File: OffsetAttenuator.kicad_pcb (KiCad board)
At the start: 2 copper layers, 17 parts, among them J1 Conn_Coaxial, J2 Conn_Coaxial, SW1 POWER, SW2 BYPASS, U1 L7805, X1 4MHz

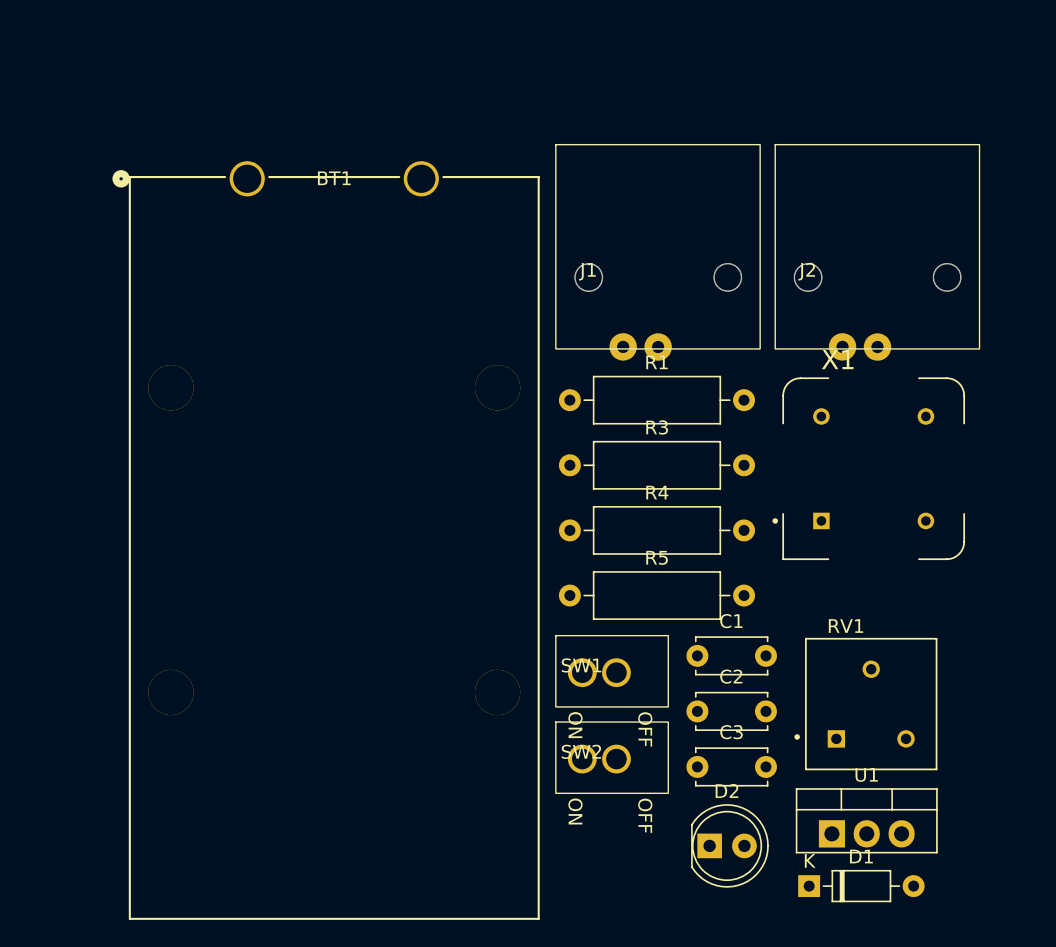
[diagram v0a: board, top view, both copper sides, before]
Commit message: adding osc schematic and footprint
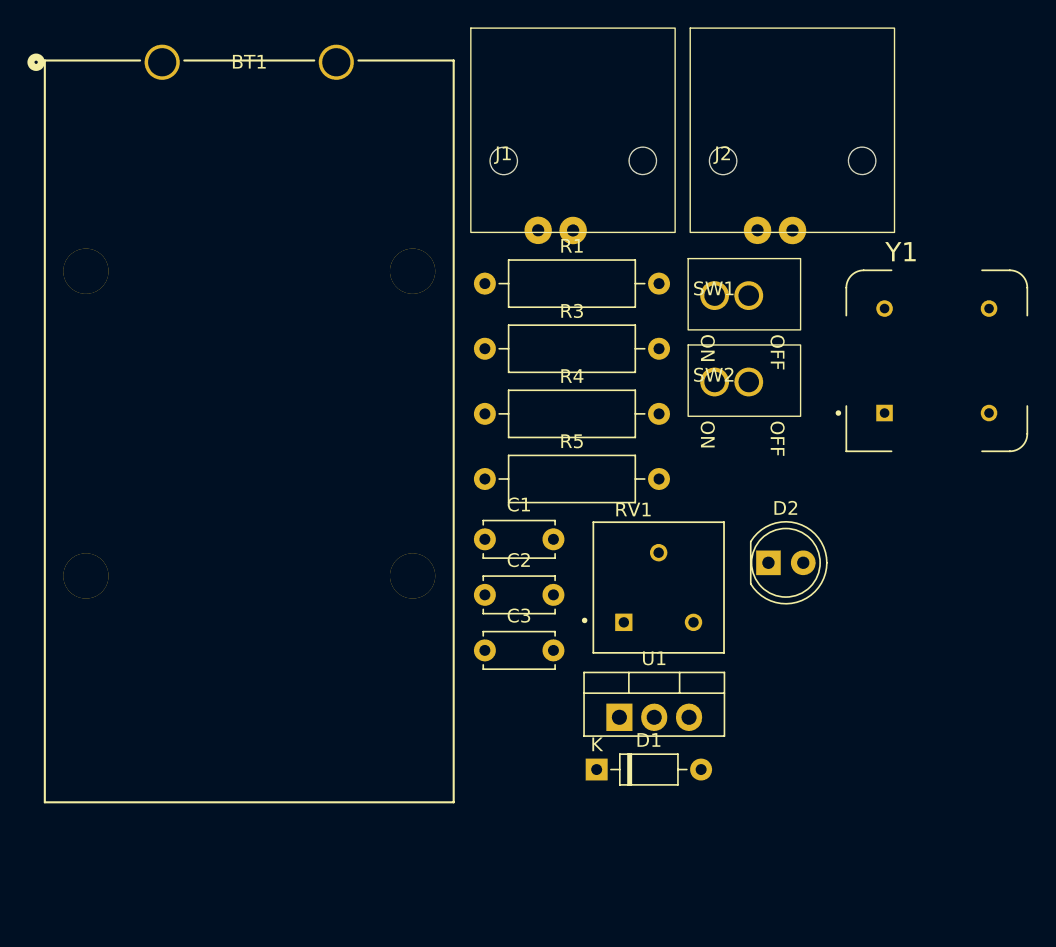
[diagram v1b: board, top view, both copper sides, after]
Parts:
- removed X1: 4MHz, Library:OSC_ECS-2100AX-040
- added Y1: ECS-2100AX-040, Library:OSC_ECS-2100AX-040, F.Cu at (163.2, 83.2)
- moved SW1 29.1 mm to (146.9, 78.4)
- moved SW2 29.1 mm to (146.9, 84.7)
- moved D2 21.1 mm to (150.9, 97.9)
- moved C1 17.7 mm to (130.2, 96.2)
- moved C2 17.7 mm to (130.2, 100.3)
- moved C3 17.7 mm to (130.2, 104.3)
- moved D1 17.7 mm to (138.4, 113.0)
- moved RV1 17.7 mm to (142.9, 99.7)
- moved U1 17.7 mm to (140.0, 109.2)
- moved J1 10.5 mm to (131.6, 68.6)
- moved J2 10.5 mm to (147.6, 68.6)
- moved R1 10.5 mm to (130.2, 77.6)
- moved R3 10.5 mm to (130.2, 82.3)
- moved R4 10.5 mm to (130.2, 87.1)
- moved R5 10.5 mm to (130.2, 91.8)
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
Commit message: begin layout
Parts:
- R4: moved to B.Cu
- moved J1 91.0 mm to (41.8, 54.0), turned to 90 degrees
- moved SW2 86.2 mm to (77.1, 34.2), turned to 90 degrees
- moved C1 80.0 mm to (63.5, 52.0), turned to 90 degrees
- moved SW1 75.8 mm to (78.5, 111.0), turned to 90 degrees
- moved D1 75.7 mm to (100.1, 47.8), turned to 180 degrees
- moved J2 68.7 mm to (211.7, 44.0), turned to -90 degrees
- moved RV1 67.5 mm to (80.5, 74.0)
- moved R1 58.2 mm to (80.5, 47.3), turned to -90 degrees
- moved BT1 57.5 mm to (100.0, 118.5)
- moved R4 53.4 mm to (78.5, 100.2), turned to 90 degrees
- moved C2 52.7 mm to (125.2, 47.8), turned to -90 degrees
- moved R3 40.3 mm to (110.5, 47.1), turned to -90 degrees
- moved D2 37.6 mm to (183.5, 79.0)
- moved R5 37.6 mm to (162.8, 72.9)
- moved Y1 34.5 mm to (133.5, 100.8), turned to 180 degrees
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
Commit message: pcb layout
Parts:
- BT1: moved to B.Cu
- moved J2 93.5 mm to (118.2, 46.2)
- moved D2 92.6 mm to (95.8, 49.2)
- moved BT1 85.4 mm to (50.3, 49.1), turned to -90 degrees
- moved R5 60.2 mm to (104.8, 56.8), turned to -90 degrees
- moved Y1 54.2 mm to (93.8, 63.8)
- moved C3 48.6 mm to (79.8, 73.0)
- moved U1 45.5 mm to (82.8, 66.0), turned to 90 degrees
- moved C2 38.8 mm to (86.8, 52.2), turned to 90 degrees
- moved SW1 36.1 mm to (74.0, 75.2), turned to 180 degrees
- moved R3 31.5 mm to (79.2, 43.5)
- moved R4 31.4 mm to (63.2, 72.7)
- moved D1 28.2 mm to (72.5, 53.6), turned to 90 degrees
- moved R1 15.5 mm to (65.5, 43.5)
- moved RV1 13.5 mm to (72.2, 63.3)
- moved C1 7.43 mm to (58.0, 47.0), turned to -90 degrees
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
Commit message: pcb layout
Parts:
- BT1: footprint Library:1294PCB_29P57X53P85_KEY -> Connector_PinHeader_2.54mm:PinHeader_1x02_P2.54mm_Vertical
- moved R4 26.8 mm to (62.0, 45.9), turned to -90 degrees
- moved SW1 26.3 mm to (53.3, 59.0), turned to 90 degrees
- moved BT1 23.8 mm to (52.8, 72.7), turned to 180 degrees
- moved SW2 21.0 mm to (53.5, 43.7), turned to -90 degrees
- moved C1 14.0 mm to (57.0, 33.0)
- moved C2 14.0 mm to (85.8, 38.3)
- moved C3 14.0 mm to (78.8, 59.0)
- moved D2 14.0 mm to (94.8, 35.3)
- moved R5 14.0 mm to (103.8, 42.8)
- moved U1 14.0 mm to (81.8, 52.0)
- moved Y1 14.0 mm to (92.8, 49.9)
- moved R1 14.0 mm to (64.5, 29.6)
- moved R3 14.0 mm to (78.2, 29.6)
- moved D1 14.0 mm to (71.5, 39.7)
- moved RV1 14.0 mm to (71.2, 49.3)
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
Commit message: more layout
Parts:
- BT1: moved to F.Cu
- moved SW2 5.20 mm to (53.0, 48.9), turned to 90 degrees
- moved C1 4.04 mm to (53.1, 32.0)
- moved R1 3.77 mm to (61.0, 28.1)
- moved J2 3.50 mm to (114.7, 46.4)
- moved R3 3.00 mm to (80.9, 28.1)
- moved C2 2.69 mm to (88.1, 37.0)
- moved R5 2.66 mm to (105.0, 45.1)
- moved RV1 2.29 mm to (70.5, 51.5)
- moved U1 1.95 mm to (81.8, 54.0)
- moved Y1 1.71 mm to (93.3, 51.5)
- moved D1 1.69 mm to (70.5, 38.3)
- moved C3 1.45 mm to (78.8, 60.5)
- moved R4 1.25 mm to (61.0, 45.1)
- moved D2 1.10 mm to (95.5, 34.5)
- moved SW1 0.59 mm to (53.0, 58.5)
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
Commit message: begin routing
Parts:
- moved D1 0.50 mm to (71.0, 38.3)
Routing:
- net Net-(J2-In): track 0.00 -> 78.8 mm
- net Net-(BT1--): track 0.00 -> 75.2 mm
- net Net-(SW1-B): track 0.00 -> 40.2 mm
- net Net-(J1-Ext): track 0.00 -> 28.2 mm
- net /+5V: track 0.00 -> 26.9 mm
- net Net-(D1-K): track 0.00 -> 26.1 mm
- net Net-(D1-A): track 0.00 -> 23.2 mm
- net Net-(C3-Pad1): track 0.00 -> 22.0 mm
- net Net-(D2-A): track 0.00 -> 15.0 mm
- net Net-(BT1-+): track 0.00 -> 14.0 mm
- net Net-(R1-Pad2): track 0.00 -> 12.9 mm
- net Net-(Y1-OUTPUT): track 0.00 -> 7.90 mm
- added copper zone on B.Cu, net GND
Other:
- board outline added: 92.5 x 65 mm

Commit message: adding mounting holes
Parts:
- added REF**: MountingHole_2.7mm_M2.5, MountingHole:MountingHole_2.7mm_M2.5, F.Cu at (121.0, 81.0)
- added REF**: MountingHole_2.7mm_M2.5, MountingHole:MountingHole_2.7mm_M2.5, F.Cu at (35.5, 23.0)
- added REF**: MountingHole_2.7mm_M2.5, MountingHole:MountingHole_2.7mm_M2.5, F.Cu at (121.0, 23.0)
- added REF**: MountingHole_2.7mm_M2.5, MountingHole:MountingHole_2.7mm_M2.5, F.Cu at (35.5, 81.0)
- R4: moved to F.Cu
